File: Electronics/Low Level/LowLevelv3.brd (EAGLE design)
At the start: 117.1 x 67.6 mm, 71 parts, among them IC1_2515 MCP2515, IC2_2551 MCP2551DIL08, IC3_4802 MCP4802, Q1 16MHz, T1 2N3904, T2 2N3904, X1 284512-4, X3 Motor, X4 CLICK

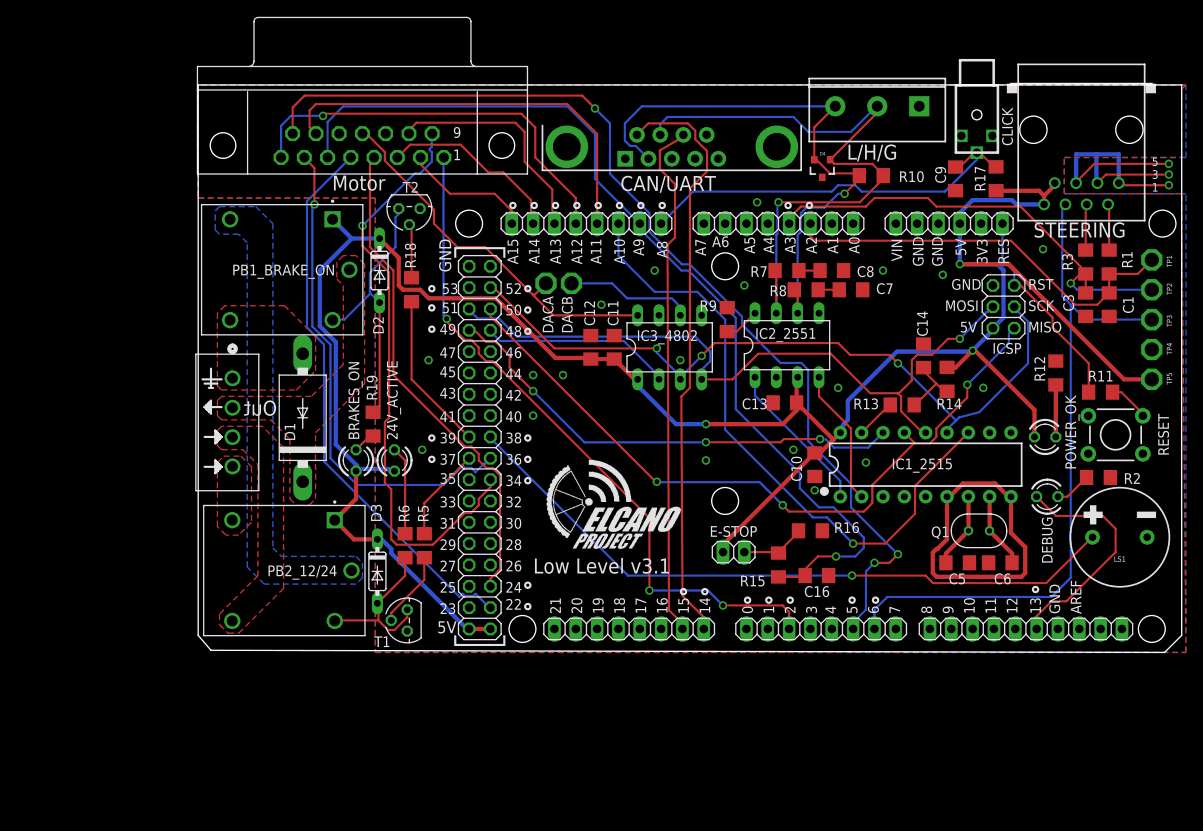
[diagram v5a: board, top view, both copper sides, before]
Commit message: Restored DACB to the DB15, but now on pin 15. Removed watchdog from DB15.
Minor changes to silkscreen and trace routing.
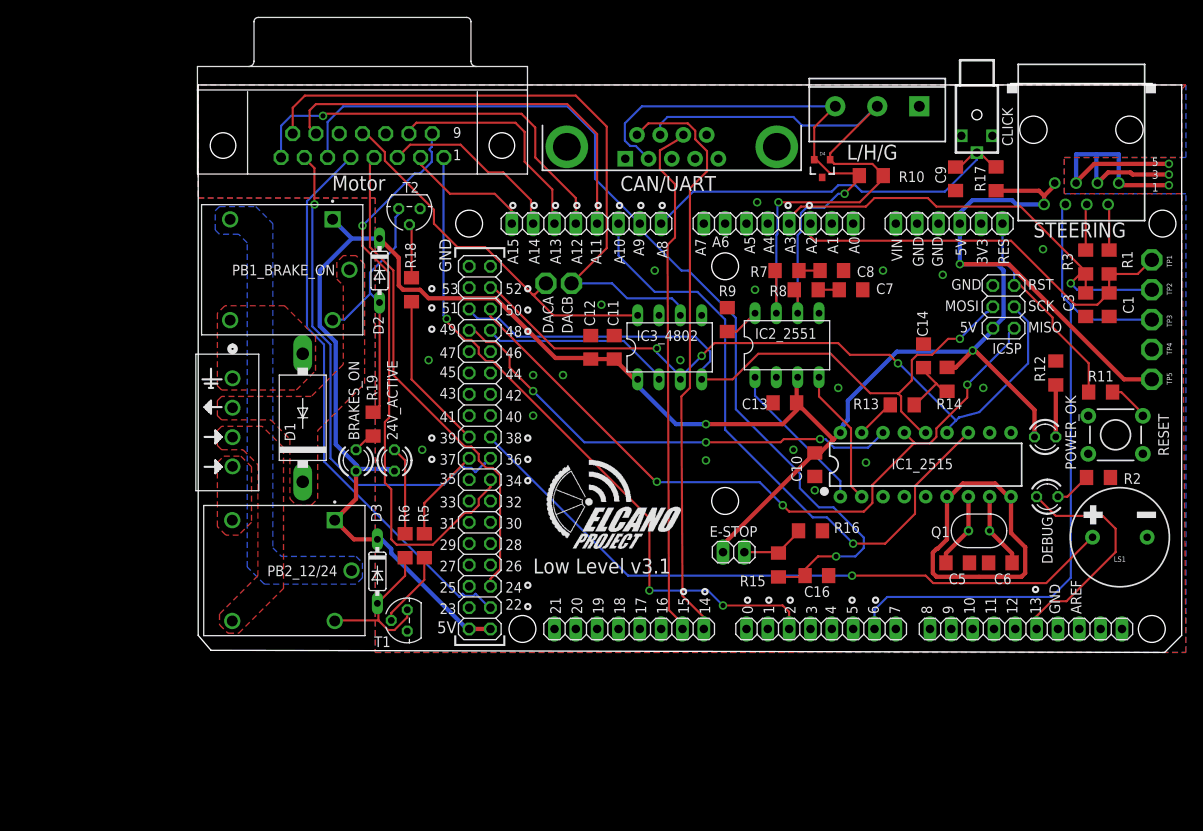
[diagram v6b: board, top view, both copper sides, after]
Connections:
- removed net WATCHDOG: DIGITAL_0-7.6, X3.15
- net DACB: now also X3.15
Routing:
- net WATCHDOG: track 122.5 -> 0.00 mm, vias 3 -> 0
- net DACB: track 15.1 -> 78.1 mm
- net CANH: track 77.9 -> 77.2 mm
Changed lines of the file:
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@@
 <vertex x="5.715" y="3.937"/>
 <vertex x="11.43" y="9.652"/>
-<vertex x="11.43" y="17.018"/>
-<vertex x="15.494" y="21.082"/>
+<vertex x="11.43" y="16.002"/>
+<vertex x="15.494" y="20.066"/>
 <vertex x="15.494" y="28.448"/>
 <vertex x="20.574" y="33.528"/>
@@
 <vertex x="20.32" y="33.782"/>
 <vertex x="15.24" y="28.702"/>
-<vertex x="15.24" y="21.336"/>
-<vertex x="10.922" y="17.018"/>
+<vertex x="15.24" y="20.066"/>
+<vertex x="10.922" y="15.748"/>
 <vertex x="10.922" y="9.398"/>
 <vertex x="5.588" y="4.064"/>
@@
 <text x="8.636" y="26.924" size="1.778" layer="26" rot="MR0">12</text>
 <text x="8.636" y="23.622" size="1.778" layer="26" rot="MR0">24</text>
-<text x="9.398" y="30.48" size="1.778" layer="25" rot="MR0">Out</text>
+<text x="9.398" y="30.48" size="1.778" layer="26" rot="MR0">Out</text>
 <text x="4.826" y="35.814" size="1.778" layer="26" rot="MR180">GND</text>
 <rectangle x1="0" y1="38.354" x2="10.668" y2="39.116" layer="26"/>
@@
 </element>
 <element name="R9" library="resistor" library_urn="urn:adsk.eagle:library:348" package="R1206" package3d_urn="urn:adsk.eagle:package:23540/2" value="4.7K" x="62.992" y="41.91" smashed="yes" rot="R90">
-<attribute name="NAME" x="59.69" y="42.926" size="1.27" layer="25" ratio="10"/>
+<attribute name="NAME" x="61.976" y="44.704" size="1.27" layer="25" ratio="10"/>
 <attribute name="VALUE" x="64.389" y="43.4086" size="0.635" layer="27" ratio="10" rot="R270"/>
 </element>
@@
 <wire x1="94.88630625" y1="22.4028" x2="96.46110625" y2="20.828" width="0.508" layer="1" locked="yes"/>
 <via x="81.534" y="47.752" extent="1-16" drill="0.6096"/>
-<via x="65.024" y="45.974" extent="1-16" drill="0.6096"/>
+<via x="66.294" y="45.466" extent="1-16" drill="0.6096"/>
 <via x="88.646" y="47.244" extent="1-16" drill="0.6096"/>
 <via x="73.406" y="21.59" extent="1-16" drill="0.6096"/>
@@
 <wire x1="106.934" y1="61.595" x2="104.521" y2="61.595" width="0.508" layer="16"/>
 <wire x1="106.934" y1="61.595" x2="106.934" y2="58.293" width="0.508" layer="16"/>
-<wire x1="104.521" y1="58.166" x2="104.521" y2="58.293" width="0.254" layer="1"/>
-<wire x1="104.521" y1="58.293" x2="106.68" y2="60.452" width="0.254" layer="1"/>
-<wire x1="106.68" y1="60.452" x2="115.57" y2="60.452" width="0.254" layer="1"/>
-<wire x1="107.061" y1="58.166" x2="108.077" y2="59.182" width="0.254" layer="1"/>
-<wire x1="108.077" y1="59.182" x2="115.57" y2="59.182" width="0.254" layer="1"/>
-<wire x1="115.57" y1="57.912" x2="109.855" y2="57.912" width="0.254" layer="1"/>
-<wire x1="109.601" y1="58.166" x2="109.855" y2="57.912" width="0.254" layer="1"/>
+<wire x1="104.521" y1="58.166" x2="104.521" y2="58.293" width="0.508" layer="1"/>
+<wire x1="104.521" y1="58.293" x2="106.68" y2="60.452" width="0.508" layer="1"/>
+<wire x1="106.68" y1="60.452" x2="115.57" y2="60.452" width="0.508" layer="1"/>
+<wire x1="107.061" y1="58.166" x2="108.331" y2="59.436" width="0.508" layer="1"/>
+<wire x1="111.252" y1="59.182" x2="115.57" y2="59.182" width="0.508" layer="1"/>
+<wire x1="111.252" y1="59.182" x2="110.998" y2="59.436" width="0.508" layer="1"/>
+<wire x1="110.998" y1="59.436" x2="108.331" y2="59.436" width="0.508" layer="1"/>
+<wire x1="115.57" y1="57.912" x2="109.855" y2="57.912" width="0.508" layer="1"/>
+<wire x1="109.601" y1="58.166" x2="109.855" y2="57.912" width="0.508" layer="1"/>
 <via x="115.57" y="60.452" extent="1-16" drill="0.6096"/>
 <via x="115.57" y="59.182" extent="1-16" drill="0.6096"/>
@@
 <wire x1="57.404" y1="43.434" x2="56.388" y2="44.45" width="0.254" layer="16"/>
 <contactref element="DACB" pad="TP"/>
-</signal>
-<signal name="WATCHDOG">
 <contactref element="X3" pad="15"/>
-<contactref element="DIGITAL_0-7" pad="6"/>
-<wire x1="12.6754625" y1="68.58" x2="11.2522" y2="67.1567375" width="0.254" layer="1"/>
-<wire x1="11.2522" y1="64.0563" x2="11.2522" y2="67.1567375" width="0.254" layer="1"/>
-<wire x1="64.7446" y1="42.272825" x2="64.7446" y2="41.3262375" width="0.254" layer="16"/>
-<wire x1="64.7446" y1="41.3262375" x2="69.3170375" y2="36.7538" width="0.254" layer="16"/>
-<wire x1="69.3170375" y1="36.7538" x2="71.8053625" y2="36.7538" width="0.254" layer="16"/>
-<wire x1="71.8053625" y1="36.7538" x2="72.6186" y2="35.9405625" width="0.254" layer="16"/>
-<wire x1="72.6186" y1="35.9405625" x2="72.6186" y2="27.4574" width="0.254" layer="16"/>
-<wire x1="72.6186" y1="27.4574" x2="77.724" y2="22.352" width="0.254" layer="16"/>
-<wire x1="58.5188" y1="48.498625" x2="64.7446" y2="42.272825" width="0.254" layer="16"/>
-<wire x1="77.724" y1="22.352" x2="77.724" y2="19.558" width="0.254" layer="16"/>
-<wire x1="77.724" y1="19.558" x2="83.312" y2="13.97" width="0.254" layer="16"/>
-<via x="83.312" y="13.97" extent="1-16" drill="0.6096"/>
-<wire x1="83.312" y1="13.97" x2="82.296" y2="12.954" width="0.254" layer="1"/>
-<wire x1="82.296" y1="12.954" x2="80.518" y2="12.954" width="0.254" layer="1"/>
-<via x="80.518" y="12.954" extent="1-16" drill="0.6096"/>
-<wire x1="79.502" y1="7.366" x2="77.978" y2="5.842" width="0.254" layer="16"/>
-<wire x1="77.978" y1="5.842" x2="77.978" y2="5.08" width="0.254" layer="16"/>
-<wire x1="80.518" y1="12.954" x2="79.502" y2="11.938" width="0.254" layer="16"/>
-<wire x1="79.502" y1="11.938" x2="79.502" y2="7.366" width="0.254" layer="16"/>
-<wire x1="53.721" y1="54.57545" x2="49.022" y2="59.27445" width="0.254" layer="16"/>
-<wire x1="53.721" y1="54.57545" x2="53.721" y2="52.35855" width="0.254" layer="16"/>
-<wire x1="49.022" y1="65.278" x2="47.244" y2="67.056" width="0.254" layer="16"/>
-<via x="47.244" y="67.056" extent="1-16" drill="0.6096"/>
-<wire x1="47.244" y1="67.056" x2="45.72" y2="68.58" width="0.254" layer="1"/>
-<wire x1="49.022" y1="59.27445" x2="49.022" y2="65.278" width="0.254" layer="16"/>
-<wire x1="45.72" y1="68.58" x2="12.6754625" y2="68.58" width="0.254" layer="1"/>
-<wire x1="53.721" y1="52.35855" x2="57.580925" y2="48.498625" width="0.254" layer="16"/>
-<wire x1="57.580925" y1="48.498625" x2="58.5188" y2="48.498625" width="0.254" layer="16"/>
+<wire x1="11.2522" y1="64.0563" x2="11.2522" y2="67.1322" width="0.254" layer="1"/>
+<wire x1="11.2522" y1="67.1322" x2="12.7" y2="68.58" width="0.254" layer="1"/>
+<wire x1="12.7" y1="68.58" x2="44.958" y2="68.58" width="0.254" layer="1"/>
+<wire x1="48.641" y1="64.897" x2="48.641" y2="50.419" width="0.254" layer="1"/>
+<wire x1="44.958" y1="68.58" x2="48.641" y2="64.897" width="0.254" layer="1"/>
+<wire x1="48.641" y1="50.419" x2="44.45" y2="46.228" width="0.254" layer="1"/>
 </signal>
 <signal name="WHEELROTATION">
@@
 <contactref element="CAN_HEADER" pad="2"/>
 <contactref element="R10" pad="2"/>
-<wire x1="80.852" y1="67.31" x2="80.852" y2="66.551" width="0.254" layer="1"/>
-<wire x1="80.852" y1="66.551" x2="75.245" y2="60.944" width="0.254" layer="1"/>
+<wire x1="80.852" y1="67.31" x2="80.849" y2="67.31" width="0.254" layer="1"/>
+<wire x1="80.849" y1="67.31" x2="75.245" y2="61.706" width="0.254" layer="1"/>
+<wire x1="75.245" y1="61.706" x2="75.245" y2="60.944" width="0.254" layer="1"/>
 <wire x1="75.245" y1="60.944" x2="75.737" y2="60.452" width="0.254" layer="1"/>
 <wire x1="75.737" y1="60.452" x2="80.264" y2="60.452" width="0.254" layer="1"/>
@@
 <wire x1="55.008" y1="65.168" x2="55.88" y2="66.04" width="0.254" layer="16"/>
 <wire x1="55.88" y1="66.04" x2="70.866" y2="66.04" width="0.254" layer="16"/>
-<wire x1="70.866" y1="66.04" x2="72.644" y2="64.262" width="0.254" layer="16"/>
-<wire x1="72.644" y1="64.262" x2="77.724" y2="64.262" width="0.254" layer="16"/>
+<wire x1="70.866" y1="66.04" x2="71.882" y2="65.024" width="0.254" layer="16"/>
+<wire x1="71.882" y1="65.024" x2="78.486" y2="65.024" width="0.254" layer="16"/>
 <wire x1="80.772" y1="67.31" x2="80.852" y2="67.31" width="0.254" layer="16"/>
-<wire x1="77.724" y1="64.262" x2="80.772" y2="67.31" width="0.254" layer="16"/>
+<wire x1="78.486" y1="65.024" x2="80.772" y2="67.31" width="0.254" layer="16"/>
 </signal>
 <signal name="CANL">
@@
 <vertex x="10.922" y="20.574"/>
 <vertex x="11.684" y="19.812"/>
-<vertex x="13.208" y="19.812"/>
-<vertex x="13.97" y="20.574"/>
-<vertex x="13.97" y="28.448"/>
+<vertex x="13.462" y="19.812"/>
+<vertex x="14.224" y="20.574"/>
+<vertex x="14.224" y="28.702"/>
 <vertex x="19.812" y="34.29"/>
 <vertex x="19.812" y="48.514"/>
@@
 <mfgpreviewcolor name="substratecolor" color="0xFF786E46"/>
 </mfgpreviewcolors>
-<errors>
-</errors>
 </board>
 </drawing>
